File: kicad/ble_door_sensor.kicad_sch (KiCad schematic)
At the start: 42 parts, among them J1 Prog Header, J101 Conn_01x08, SW101 SW_Reed, SW102 SW_Push, SW103 REED_EXT, SW104 REED_EXT, SW105 REED_EXT, U1 nRF52832-QFxx, Y1 Crystal_GND24

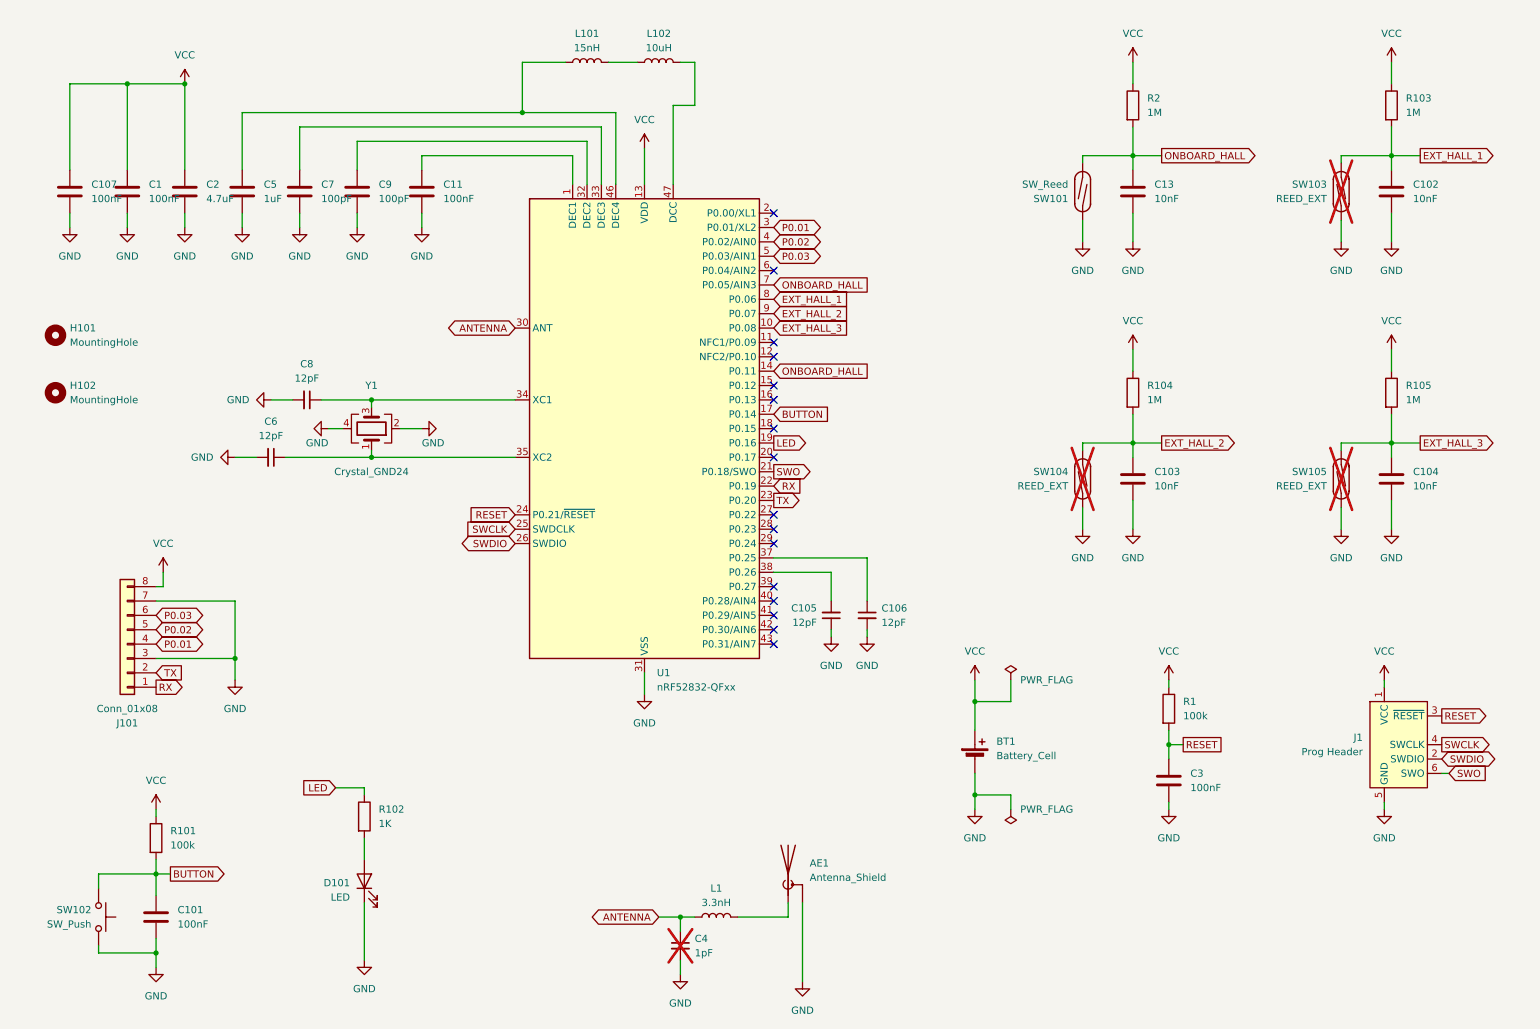
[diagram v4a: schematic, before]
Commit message: Add Temperature sensor instead of external reed
Remove the contacts fro external reed contacts
Add temperature sensor
Reduce the size of the PCB
Add additional mounting hole
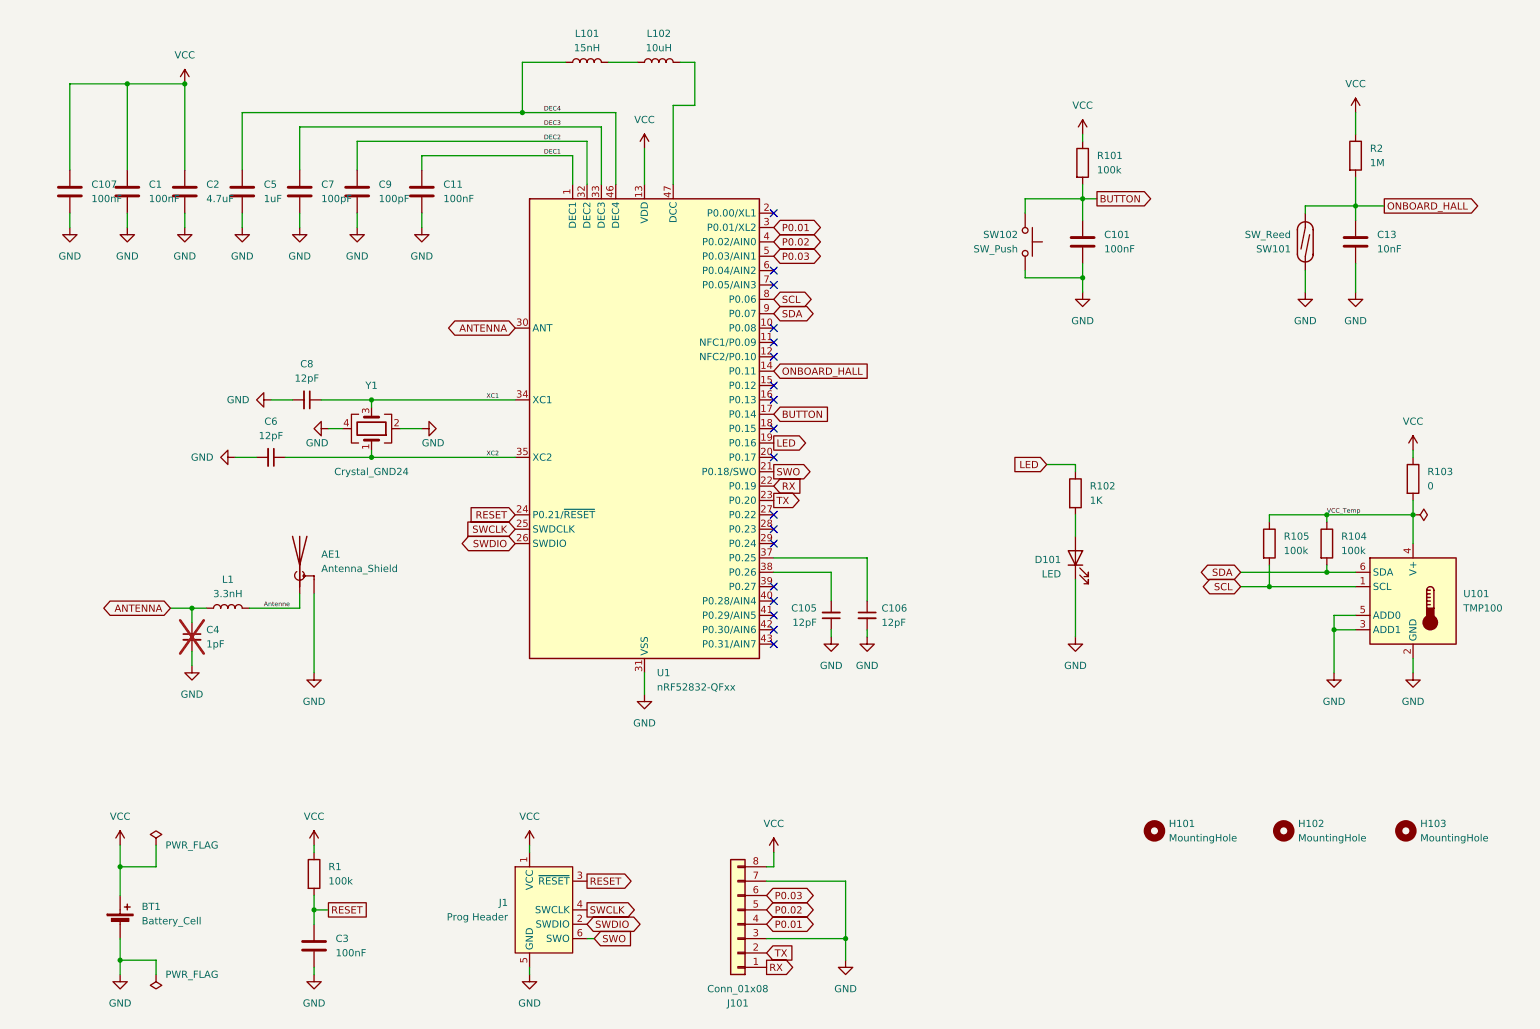
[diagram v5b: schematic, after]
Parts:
- removed C102, C103, C104: 10nF, Capacitor_SMD:C_0402_1005Metric, symbol Device:C
- removed SW103, SW104, SW105: REED_EXT, Connector_PinHeader_1.00mm:PinHeader_1x02_P1.00mm_Vertical, symbol Switch:SW_Reed
- added H103: MountingHole, MountingHole:MountingHole_2.2mm_M2, symbol Mechanical:MountingHole
- added U101: TMP100, Package_TO_SOT_SMD:SOT-23-6, symbol Sensor_Temperature:TMP100
- R102: footprint Resistor_SMD:R_0603_1608Metric -> Resistor_SMD:R_0402_1005Metric; LCSC# C21190 -> C11702
- R103: value 1M -> 0; footprint Resistor_SMD:R_0402_1005Metric -> Resistor_SMD:R_0603_1608Metric; LCSC# C26083 -> C21189
- R104, R105: value 1M -> 100k; LCSC# C26083 -> C25741
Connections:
- net GND: now also U101.2 (GND), U101.3 (ADD1), U101.5 (ADD0)
- net ONBOARD_HALL: no longer U1.7 (P0.05/AIN3)
- net VCC: no longer R104.1, R105.1
- net Antenne: now reaches AE1.1 (A), L1.2
- net DEC1: now reaches C11.1, U1.1 (DEC1)
- net DEC4: now reaches C5.1, L101.1, U1.46 (DEC4)
- net XC2: now reaches C6.1, U1.35 (XC2), Y1.1
- net DEC3: now reaches C7.1, U1.33 (DEC3)
- net XC1: now reaches C8.1, U1.34 (XC1), Y1.3
- net DEC2: now reaches C9.1, U1.32 (DEC2)
- net EXT_HALL_1 renamed SCL
- net SCL: now also R105.2, U101.1 (SCL); no longer R103.2
- net EXT_HALL_2 renamed SDA
- net SDA: now also U101.6 (SDA)
- net EXT_HALL_3: no longer names the net of U1.10 (P0.08)
- net EXT_HALL_3: no longer R105.2
- new net VCC_Temp: R103.2, R104.1, R105.1, U101.4 (V+)
- no-connect marks 16 -> 18
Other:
- moved on the sheet: AE1, BT1, C101, C13, C3, C4, D101, H101, H102, J1, J101, L1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

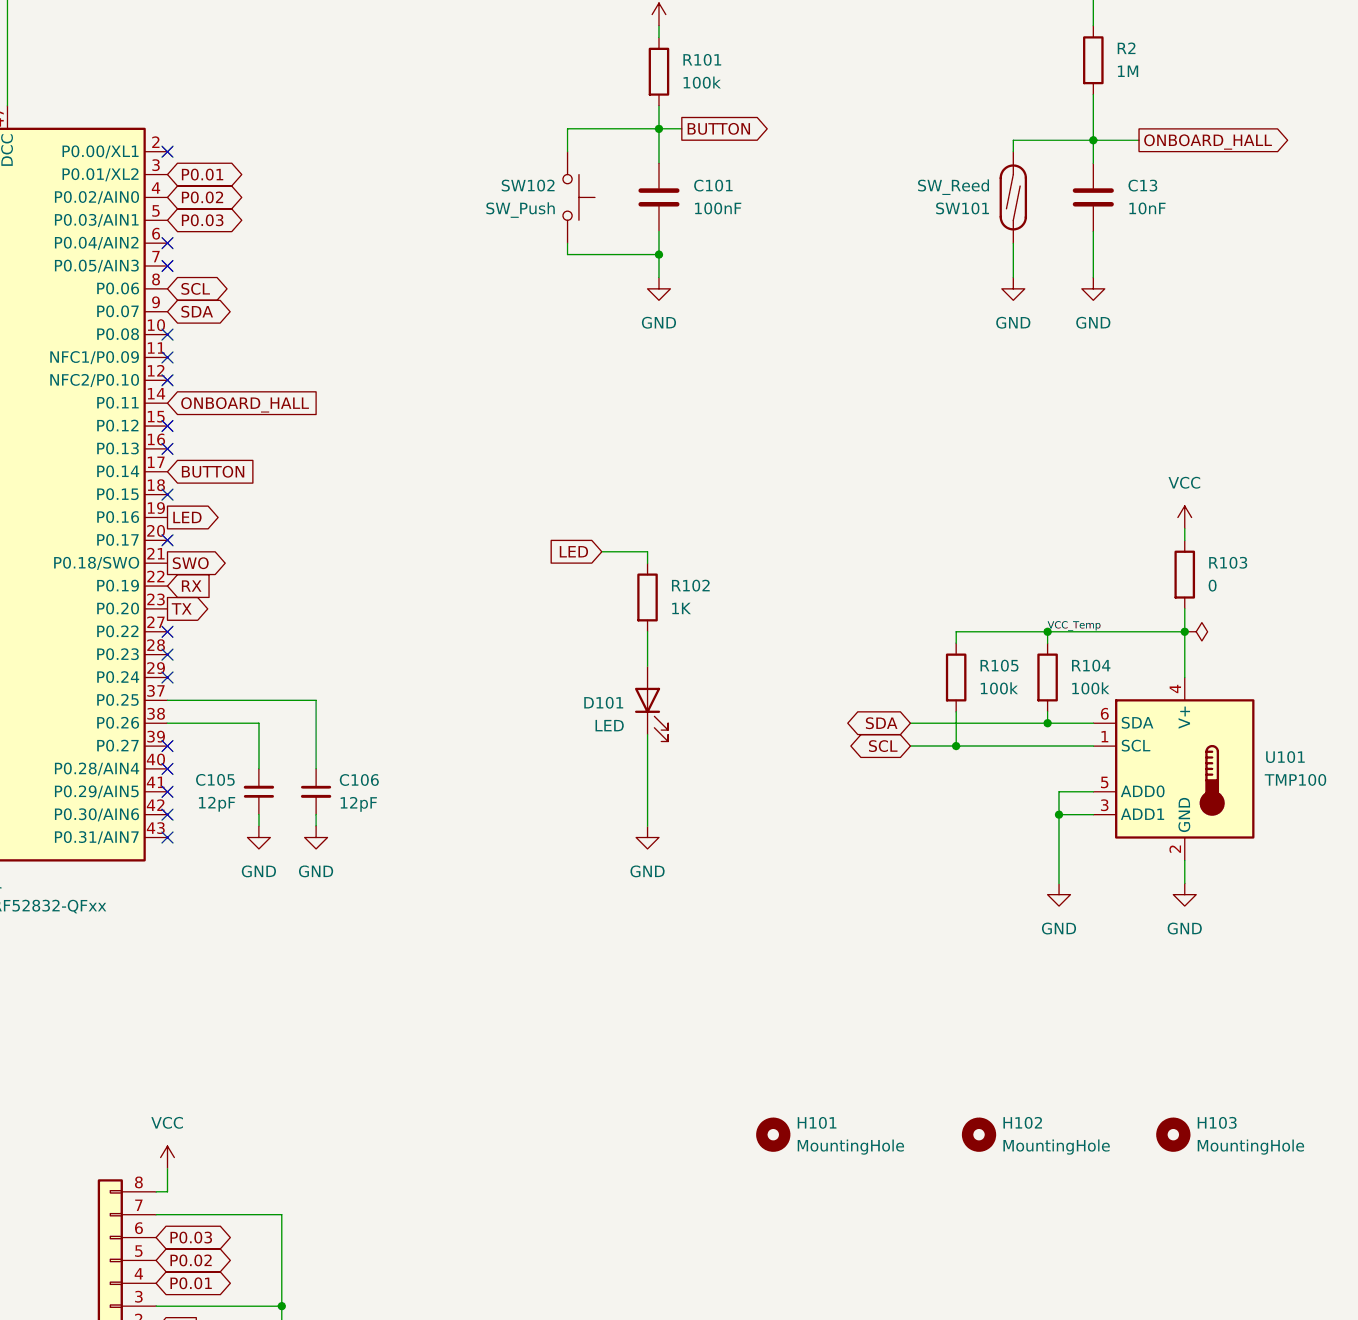
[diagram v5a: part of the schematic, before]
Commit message: Add tmp100 sensor for temperature
also added mounting holes for assembly machines
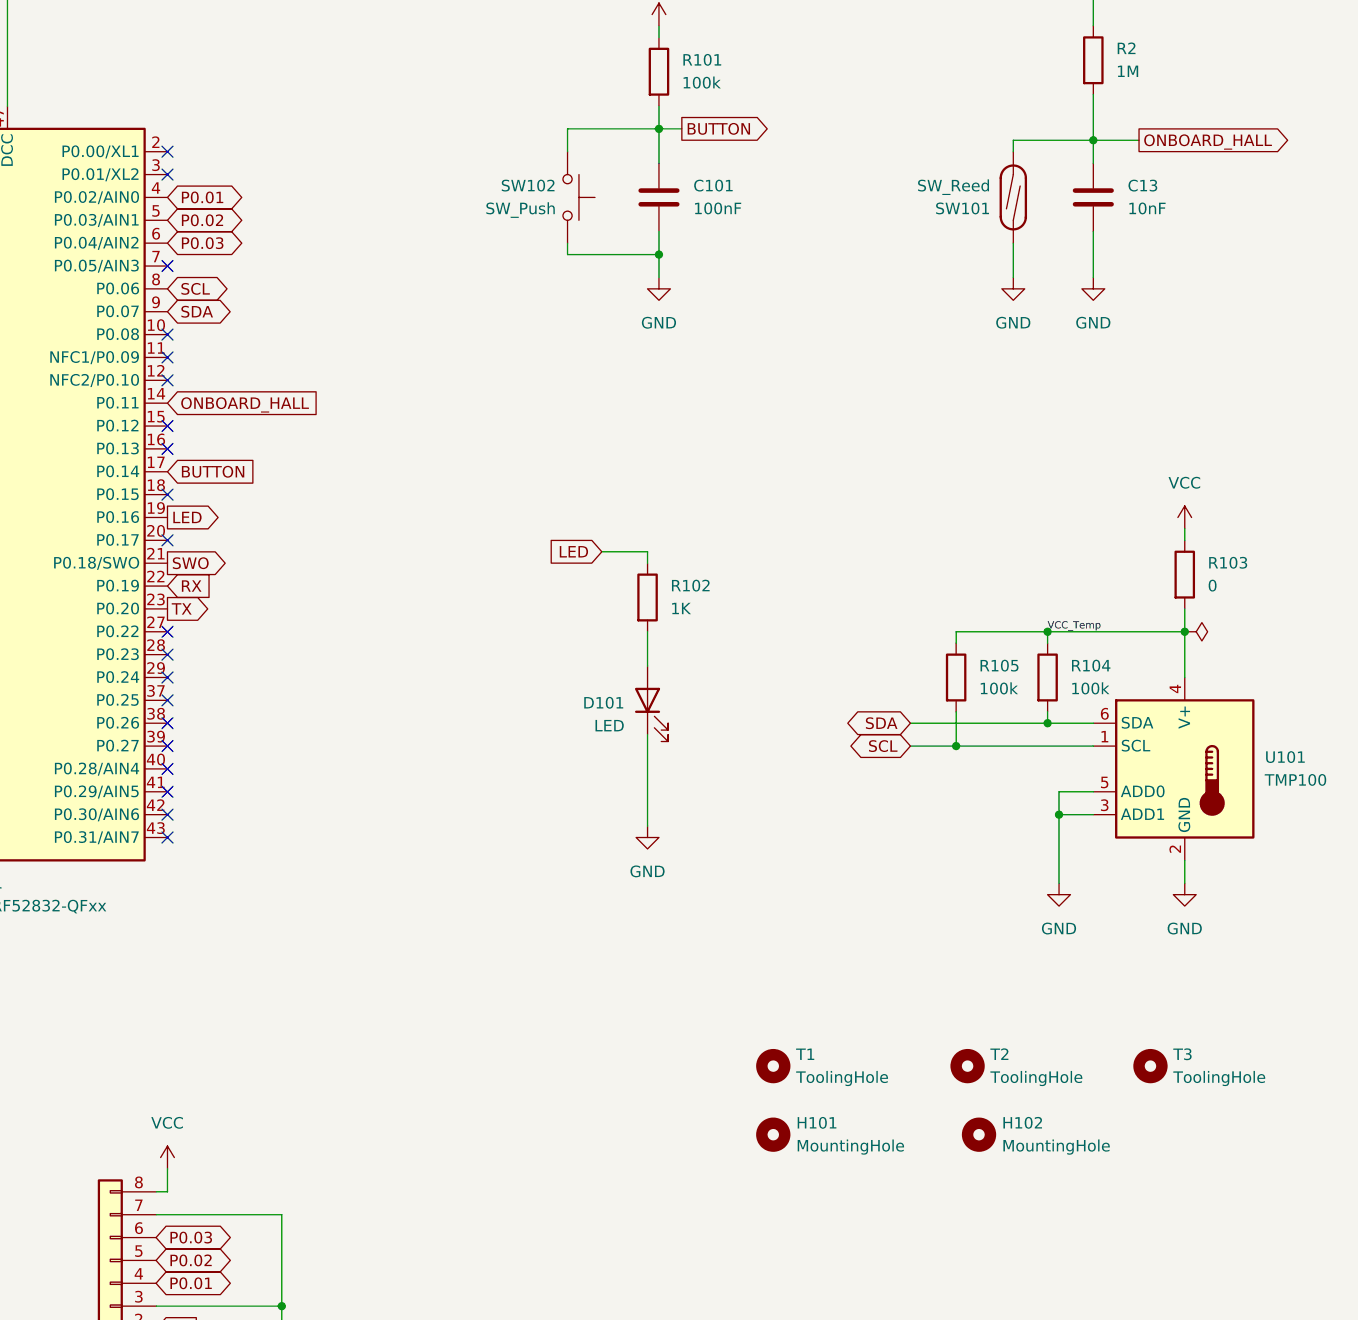
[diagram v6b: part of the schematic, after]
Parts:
- removed C105, C106: 12pF, Capacitor_SMD:C_0402_1005Metric, symbol Device:C_Small
- removed H103: MountingHole, MountingHole:MountingHole_2.2mm_M2, symbol Mechanical:MountingHole
- added T1, T2, T3: ToolingHole, Library:JLCPCB_Mounting_hole, symbol Mechanical:MountingHole
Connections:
- net P0.01: now also U1.4 (P0.02/AIN0); no longer U1.3 (P0.01/XL2)
- net P0.02: now also U1.5 (P0.03/AIN1); no longer U1.4 (P0.02/AIN0)
- net P0.03: now also U1.6 (P0.04/AIN2); no longer U1.5 (P0.03/AIN1)
- no-connect marks 18 -> 20
